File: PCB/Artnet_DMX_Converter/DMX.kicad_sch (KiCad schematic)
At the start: 45 parts, among them J10 XLR5, J11 XLR3, J4 XLR5, J5 XLR3, J6 XLR5, J7 XLR3, J8 XLR5, J9 XLR3, U10 MAX3485, U11 MAX3485, U12 TXS0101DCK, U8 MAX3485, U9 MAX3485

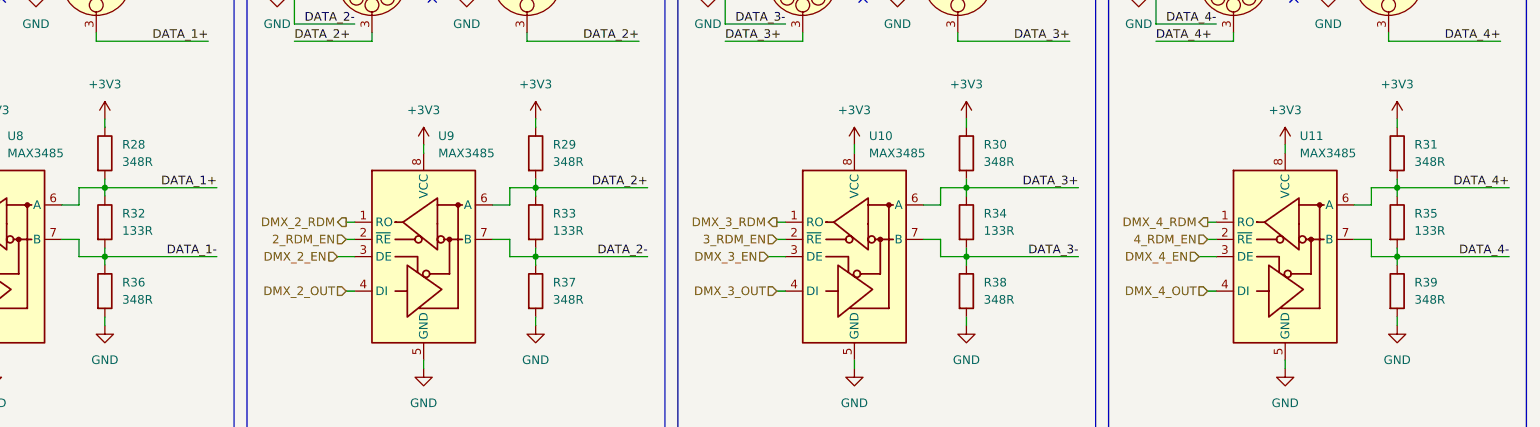
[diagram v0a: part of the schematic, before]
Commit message: Updated the PCB Allot
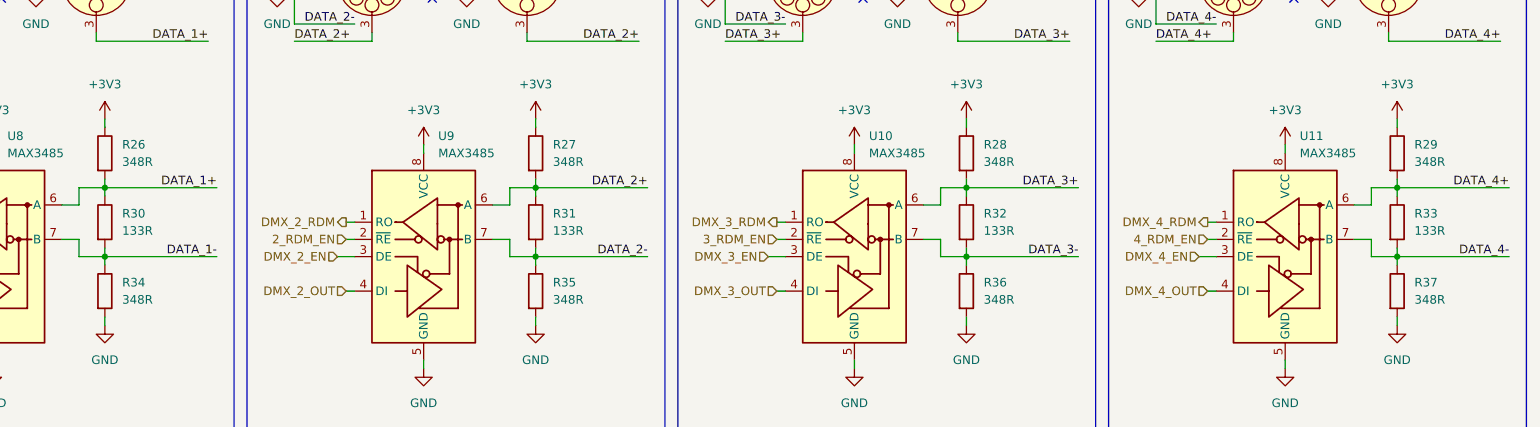
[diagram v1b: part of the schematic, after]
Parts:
- renumbered R28 to R26, R29 to R27, R30 to R28, R31 to R29, R32 to R30, R33 to R31, R34 to R32, R35 to R33, R36 to R34, R37 to R35, R38 to R36, R39 to R37
